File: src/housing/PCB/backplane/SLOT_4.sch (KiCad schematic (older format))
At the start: 1 part, among them J5 10018784-10201TLF

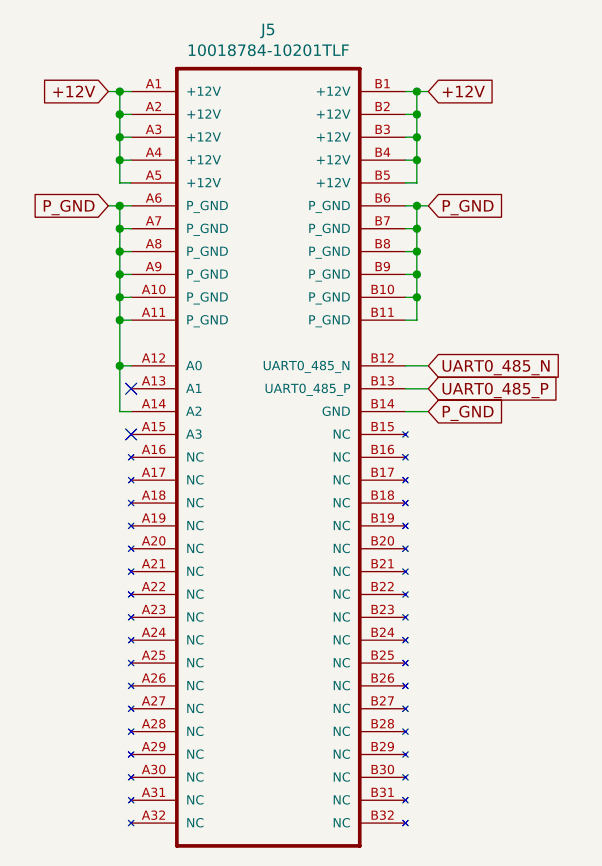
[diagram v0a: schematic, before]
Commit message: fixing backplane libraries path error
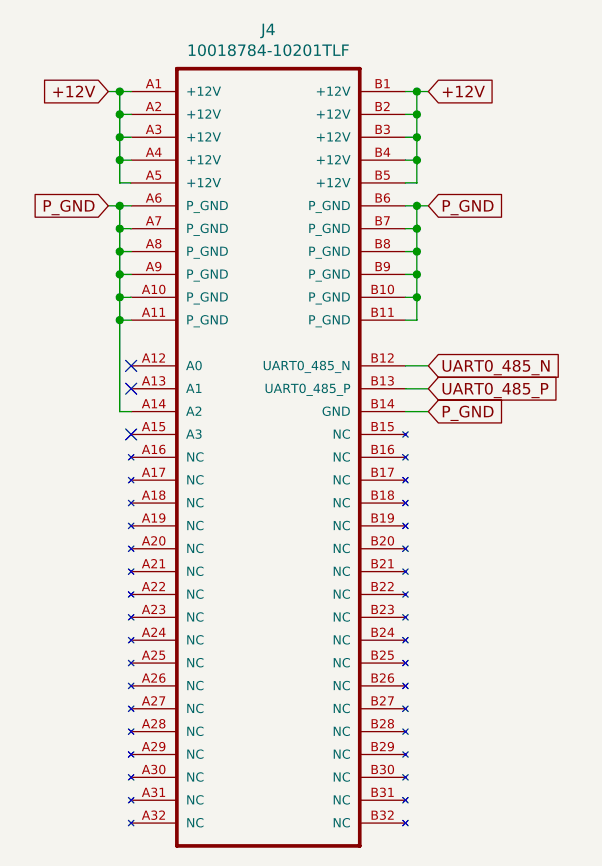
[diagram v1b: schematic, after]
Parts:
- removed J5: 10018784-10201TLF, kicad-lib:CONN_10018784-10201TLF, symbol 10018784-10201TLF:10018784-10201TLF
- added J4: 10018784-10201TLF, kicad-lib:CONN_10018784-10201TLF, symbol 10018784-10201TLF:10018784-10201TLF
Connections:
- net +12V: now also J4.A1 (+12V), J4.A2 (+12V), J4.A3 (+12V), J4.A4 (+12V), J4.A5 (+12V), J4.B1 (+12V), J4.B2 (+12V), J4.B3 (+12V), J4.B4 (+12V), J4.B5 (+12V)
- net P_GND: now also J4.A10 (P_GND), J4.A11 (P_GND), J4.A14 (A2), J4.A6 (P_GND), J4.A7 (P_GND), J4.A8 (P_GND), J4.A9 (P_GND), J4.B10 (P_GND), J4.B11 (P_GND), J4.B14 (GND), J4.B6 (P_GND), J4.B7 (P_GND), J4.B8 (P_GND), J4.B9 (P_GND)
- net UART0_485_N: now also J4.B12 (UART0_485_N)
- net UART0_485_P: now also J4.B13 (UART0_485_P)
- no-connect marks 2 -> 3
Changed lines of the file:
@@
 $Descr A4 11693 8268
 encoding utf-8
-Sheet 6 9
-Title ""
+Sheet 5 9
+Title "ACS backplane"
 Date ""
-Rev ""
-Comp ""
-Comment1 ""
+Rev "1"
+Comp "Halidelabs"
+Comment1 "contact@halidelabs.eu"
 Comment2 ""
 Comment3 ""
@@
 $Comp
 L 10018784-10201TLF:10018784-10201TLF J?
-U 1 1 5DF52F0D
+U 1 1 5DF52F0E
 P 5600 3950
-AR Path="/5DF19C0C/5DF52F0D" Ref="J?"  Part="1"
-AR Path="/5DF2A71E/5DF52F0D" Ref="J?"  Part="1"
-AR Path="/5DF2E10A/5DF52F0D" Ref="J?"  Part="1"
-AR Path="/5DF2E1F6/5DF52F0D" Ref="J?"  Part="1"
-AR Path="/5DF2E246/5DF52F0D" Ref="J5"  Part="1"
-AR Path="/5DF2E24A/5DF52F0D" Ref="J?"  Part="1"
-F 0 "J5" H 5600 5820 50  0000 C CNN
+AR Path="/5DF19C0C/5DF52F0E" Ref="J?"  Part="1"
+AR Path="/5DF2A71E/5DF52F0E" Ref="J?"  Part="1"
+AR Path="/5DF2E10A/5DF52F0E" Ref="J?"  Part="1"
+AR Path="/5DF2E1F8/5DF52F0E" Ref="J4"  Part="1"
+AR Path="/5DF2E248/5DF52F0E" Ref="J?"  Part="1"
+AR Path="/5DF2E24C/5DF52F0E" Ref="J?"  Part="1"
+F 0 "J4" H 5600 5820 50  0000 C CNN
 F 1 "10018784-10201TLF" H 5600 5729 50  0000 C CNN
 F 2 "kicad-lib:CONN_10018784-10201TLF" H 5650 4450 50  0001 L BNN
@@
 Wire Wire Line
 	6300 3750 6200 3750
-Wire Wire Line
-	4950 3350 4950 3550
-Wire Wire Line
-	4950 3550 5000 3550
 Connection ~ 4950 3350
 Wire Wire Line
-	4950 3550 4950 3750
+	4950 3750 5000 3750
 Wire Wire Line
-	4950 3750 5000 3750
-Connection ~ 4950 3550
+	4950 3350 4950 3750
+NoConn ~ 5000 3550
 NoConn ~ 5000 3650
 NoConn ~ 5000 3850
